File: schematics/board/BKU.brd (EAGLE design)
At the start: 94 x 94 mm, 81 parts, among them Q1 8MHz, Q2 32,768KHz, U1 STM32F405RGT6

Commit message: Папка с платами
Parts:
- removed BT1: 6.8MM_COIN_CELL, SparkFun-Batteries:BATTCON-6.8MM
- removed C10, C11: 10pF, rcl:C0603
- removed C13, C9: 2,2µ, rcl:C0603
- removed C18, C2, C20, C53, C54, C55: 100nF, rcl:C0603
- removed C19: 10µ, rcl:C1206
- removed C7, C8: 27pF, rcl:C0603
- removed D1: BB141, diode:SOD523
- removed GPS: GPSNEO6M, CanCubeSat:GPS-NEO6M
- removed LED2, LED3: (no value), led:CHIPLED_0603
- removed MAG: (no value), pinheadCS:1X04
- removed Q1: 8MHz, 9C-8.000MEEJ-T:XTAL_9C-8.000MEEJ-T
- removed Q2: 32,768KHz, CanCubeSat:C005R
- removed R1, R14, R3, R7: 10k, resistor:R0603
- removed R15, R16: 2k, resistor:R0603
- removed R17: 1M, resistor:R0603
- removed R25, R26: 5k1, resistor:R0603
- removed R4: 620R, resistor:R0603
- removed U$4: USB-C, CanCubeSat:USB-C
- removed U1: STM32F405RGT6, STM32F405RGT6:QFP50P1200X1200X160-64N
- moved JP1 33.6 mm to (8.75, 15.2), turned to 90 degrees
- moved BSK2A 6.50 mm to (9.90, 53.0)
- moved R29 5.02 mm to (49.5, 41.2), turned to 180 degrees
- moved U$6 4.00 mm to (0.00, 34.0)
- moved U$8 2.97 mm to (75.2, 31.8), turned to 90 degrees
- moved BSK2 2.50 mm to (39.0, 9.90)
- moved BSK3 2.50 mm to (84.1, 47.0)
- moved BSK4 2.50 mm to (47.0, 84.1)
- moved C12 2.24 mm to (44.4, 17.2)
- moved R18 2.24 mm to (44.4, 13.0)
- moved R21 2.24 mm to (44.4, 15.1)
- moved R22 2.24 mm to (47.5, 17.2)
- moved R23 2.24 mm to (47.5, 15.1)
- moved R24 2.24 mm to (47.5, 13.0)
- moved RADIO 2.00 mm to (78.2, 41.0)
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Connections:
- removed net N$1: BT1.+, R4.1
- removed net N$15: C8.1, Q1.1, R17.1, U1.6
- removed net N$2: D1.C, R4.2, U1.1
- removed net N$30: C7.1, Q1.2, R17.2, U1.5
- removed net N$34: C10.1, Q2.P$2, U1.3
- removed net N$35: C11.1, Q2.P$1, U1.4
- removed net N$37: LED2.C, R15.2
- removed net N$38: R15.1, U1.53
- removed net N$40: LED3.C, R16.2
- removed net N$41: GPS.P$2, U1.16
- removed net N$42: GPS.P$3, U1.17
- removed net N$5: JP1.2, R14.1, U1.62
- removed net N$6: U1.54, U1.58
- removed net N$7: C9.2, U1.31
- removed net N$8: C13.2, U1.47
- removed net NRST: R7.1, U$4.NRST/EN, U1.7
- removed net RX-S: U$4.RX0, U1.51
- removed net SCL: MAG.3, R25.2, U1.29
- removed net SDA: MAG.4, R26.2, U1.30
- removed net SWC: R3.1, U$4.SWC/TXD, U1.49
- removed net SWD: R1.1, U$4.SWD/RXD, U1.46
- removed net TIME-G: GPS.P$1, U1.14, U1.23, U1.59
- removed net TX-S: U$4.TX0, U1.52
- net 5V: no longer GPS.P$5
- net DAT0: now also JP1.2
- net GND: now also JP1.1, SD.VSS; no longer BT1.-, C10.2, C11.2, C13.1, C18.1, C19.1, C2.2, C20.1, C53.1, C54.1, C55.1, C7.2, C8.2, C9.1, GPS.P$4, MAG.1, R14.2, R16.1, SD.VDD, U$4.GND0, U$4.GND1, U1.12, U1.18, U1.28, U1.60, U1.63
- net RX-ES: no longer U1.42
- net TIME-ES: no longer U1.22
- net TX-ES: no longer U1.43
- net VDD: now also SD.VDD; no longer C18.2, C19.2, C2.1, C20.2, C53.2, C54.2, C55.2, D1.A, JP1.1, LED2.A, LED3.A, MAG.2, R1.2, R25.1, R26.1, R3.2, R7.2, SD.VSS, U$4.3V3/BUS0, U$4.3V3/BUS1, U1.13, U1.19, U1.32, U1.48, U1.64
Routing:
- net 5V: track 299.4 -> 122.3 mm, vias 14 -> 8
- net VDD: track 466.6 -> 325.5 mm, vias 25 -> 17
- net GND: track 525.3 -> 404.7 mm, vias 28 -> 13
- net 1W: track 211.0 -> 103.9 mm, vias 11 -> 8
- net SDA: track 96.3 -> 0.00 mm, vias 8 -> 0
- net SCL: track 91.1 -> 0.00 mm, vias 10 -> 0
- net NRST: track 58.3 -> 0.00 mm, vias 2 -> 0
- net SCLTM: track 144.6 -> 88.9 mm, vias 6 -> 5
- net N$2: track 52.6 -> 0.00 mm, vias 6 -> 0
- net B1_KEM+: track 55.2 -> 3.43 mm, vias 4 -> 2
- net DS: track 123.4 -> 75.3 mm
- net TIME-G: track 45.6 -> 0.00 mm, vias 3 -> 0
- net B2A_KEM+: track 130.4 -> 86.9 mm, vias 7 -> 3
- net B4_KHEAT: track 55.0 -> 11.5 mm, vias 3 -> 1
- net N$15: track 41.6 -> 0.00 mm, vias 3 -> 0
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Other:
- outline, holes or cut-outs redrawn

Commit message: Сделаны платы CROSSnew, SPIDERnew, BSK2
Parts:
- removed BSK2A: (no value), pinheadCS:1X08
- added BSK1: (no value), pinheadCS:1X20
- BSK3: device pinheadCS:1X12 -> pinheadCS:1X14
- BSK4: device pinheadCS:1X14 -> pinheadCS:1X08
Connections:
- new net 3V3: BSK1.8, BSK3.8
- new net B1-CMD: BSK1.4
- new net B1-KHEAT: BSK1.1
- new net B1-KVCC: BSK1.2
- new net B1-ROZE: BSK1.3
- new net B2-CMD: BSK2.4
- new net B2-KHEAT: BSK2.1
- new net B2-KVCC: BSK2.2
- new net B2-ROZE: BSK2.3
- new net B3-CMD: BSK3.4
- new net B3-KHEAT: BSK3.1
- new net B3-KVCC: BSK3.2
- new net B3-ROZE: BSK3.3
- new net B4-CMD: BSK4.4
- new net B4-KHEAT: BSK4.1
- new net B4-KVCC: BSK4.2
- new net B4-ROZE: BSK4.3
- new net B5-CMD: BSK3.13
- new net B5-KHEAT: BSK3.10
- new net B5-KVCC: BSK3.11
- new net B5-ROZE: BSK3.12
- new net PL1-KVCC: BSK1.15
- new net PL2-KVCC: BSK1.16
- new net PL3-KVCC: BSK1.17
- new net PL4-KVCC: BSK1.18
- new net PL5-KVCC: BSK1.19
- new net PL6-KVCC: BSK1.20
- new net SCL: BSK1.10
- new net SDA: BSK1.12
- new net SINS-KVCC: BSK3.14
- net 1W: now also BSK1.5, BSK2.5, BSK3.5, BSK4.5; no longer BSK2.6, BSK2A.6, BSK3.8, BSK4.14
- net 5V: now also BSK1.7, BSK3.7, BSK4.7; no longer BSK2A.7, BSK3.9, BSK4.2
- net B2A_KEM+: no longer BSK2A.3
- net B2A_KEM-: no longer BSK2A.2
- net B2A_KHEAT: no longer BSK2A.4
- net B2A_KVCC: no longer BSK2A.5
- net B2_KEM+: no longer BSK2.3
- net B2_KEM-: no longer BSK2.2
- net B2_KHEAT: no longer BSK2.4
- net B2_KVCC: no longer BSK2.5
- net B3_KEM+: no longer BSK3.5
- net B3_KEM-: no longer BSK3.4
- net B3_KHEAT: no longer BSK3.6
- net B3_KVCC: no longer BSK3.7
- net B4_KEM+: no longer BSK4.11
- net B4_KEM-: no longer BSK4.10
- net B4_KHEAT: no longer BSK4.12
- net B4_KVCC: no longer BSK4.13
- net B5_KEM+: no longer BSK3.2
- net B5_KEM-: no longer BSK3.1
- net B5_KHEAT: no longer BSK3.11
- net B5_KVCC: no longer BSK3.12
- net BUS+: now also BSK1.6, BSK2.6, BSK3.6, BSK4.6; no longer BSK2.8, BSK2A.8, BSK3.10, BSK4.3
- net GND: now also BSK1.11, BSK1.9, BSK2.8, BSK3.9, BSK4.8; no longer BSK2.1, BSK2A.1, BSK3.3, BSK4.9
- net I2CINT: no longer BSK4.5
- net PL_KVCC: no longer BSK4.8
- net SCLTM: no longer BSK4.7
- net SDATM: no longer BSK4.6
- net TIME: now also BSK1.14; no longer BSK4.4
- net TIME-ES: now also BSK1.13
- net VDD: no longer BSK4.1
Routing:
- net GND: track 404.7 -> 378.1 mm
- net BUS+: track 334.6 -> 321.0 mm
- net B2_KEM-: track 48.8 -> 46.1 mm
- net B5_KVCC: track 45.2 -> 42.8 mm

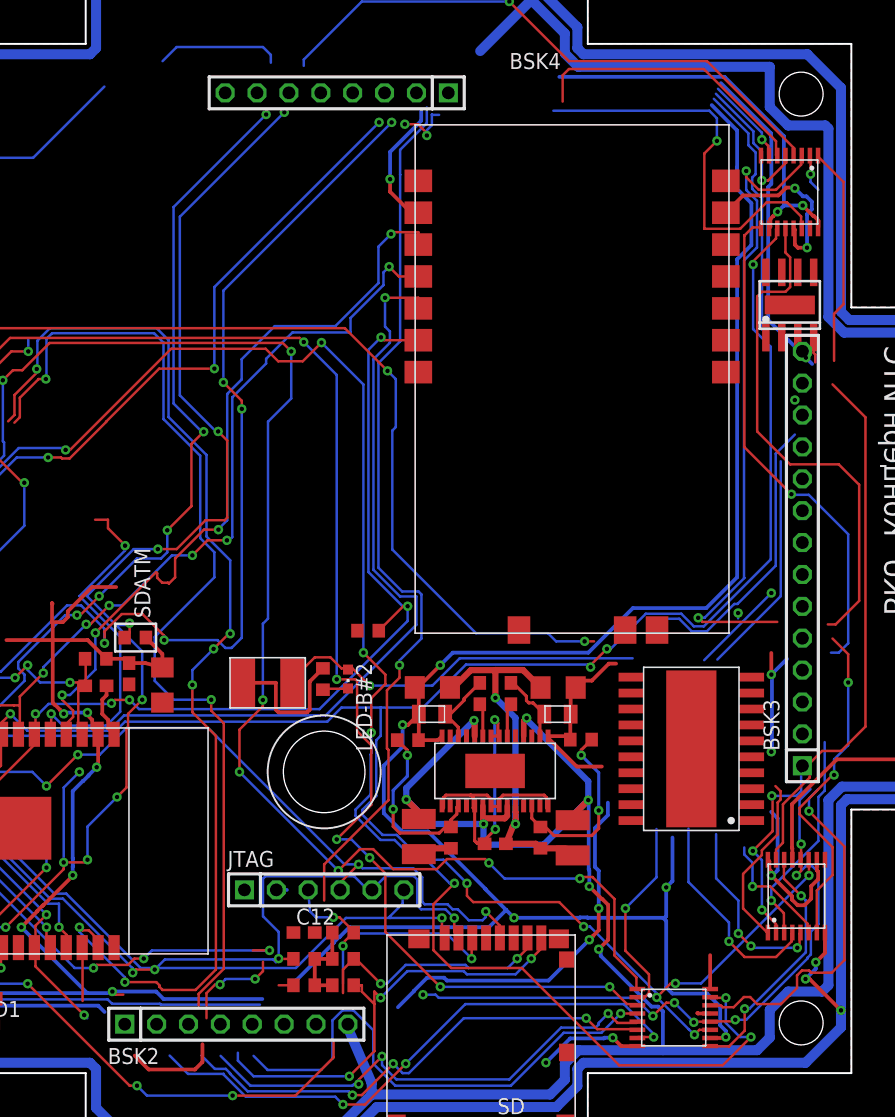
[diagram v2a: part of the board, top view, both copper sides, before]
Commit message: Разведена БСК1
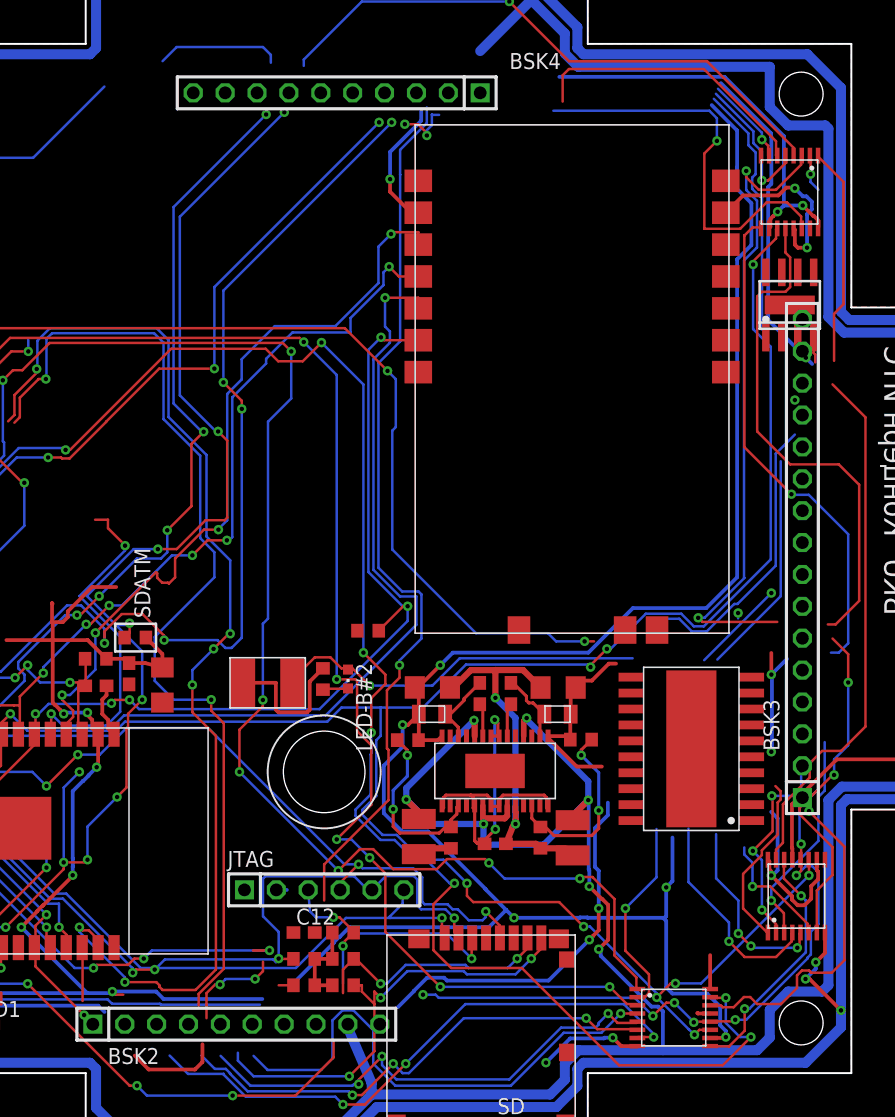
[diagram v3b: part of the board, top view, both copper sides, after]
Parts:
- BSK2, BSK4: device pinheadCS:1X08 -> pinheadCS:1X10
- BSK3: device pinheadCS:1X14 -> pinheadCS:1X16
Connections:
- removed net SCL: BSK1.10
- removed net SCLTM: R10.2, U$13.27
- removed net SDA: BSK1.12
- removed net SDATM: R11.2, U$13.28
- new net SCL-INA: BSK2.9, BSK3.15, BSK4.9
- new net SCL-TM: BSK1.10, R10.2, U$13.27
- new net SDA-INA: BSK2.10, BSK3.16, BSK4.10
- new net SDA-TM: BSK1.12, R11.2, U$13.28
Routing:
- net SDATM: track 100.3 -> 0.00 mm, vias 11 -> 0
- net SDA-TM: track 0.00 -> 100.3 mm, vias 0 -> 11
- net SCLTM: track 88.9 -> 0.00 mm, vias 5 -> 0
- net SCL-TM: track 0.00 -> 88.9 mm, vias 0 -> 5
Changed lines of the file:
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@@
 </autorouter>
 <elements>
-<element name="BSK2" library="pinheadCS" package="1X08" value="" x="39" y="9.9" smashed="yes">
+<element name="BSK2" library="pinheadCS" package="1X10" value="" x="39" y="9.9" smashed="yes">
 <attribute name="NAME" x="28.7638" y="6.7288" size="1.27" layer="25" ratio="10"/>
 <attribute name="VALUE" x="28.84" y="6.725" size="1.27" layer="27"/>
 </element>
-<element name="BSK3" library="pinheadCS" package="1X14" value="" x="84.1" y="47" smashed="yes" rot="R90">
+<element name="BSK3" library="pinheadCS" package="1X16" value="" x="84.1" y="47" smashed="yes" rot="R90">
 <attribute name="NAME" x="82.2712" y="31.6838" size="1.27" layer="25" ratio="10" rot="R90"/>
 <attribute name="VALUE" x="87.275" y="31.76" size="1.27" layer="27" rot="R90"/>
 </element>
-<element name="BSK4" library="pinheadCS" package="1X08" value="" x="47" y="84.1" smashed="yes" rot="R180">
+<element name="BSK4" library="pinheadCS" package="1X10" value="" x="47" y="84.1" smashed="yes" rot="R180">
 <attribute name="NAME" x="64.8562" y="87.2712" size="1.27" layer="25" ratio="10" rot="R180"/>
 <attribute name="VALUE" x="64.78" y="87.275" size="1.27" layer="27" rot="R180"/>
@@
 <wire x1="32.01939375" y1="6.288" x2="30.11" y2="1.2162" width="0" layer="19" extent="1-16"/>
 <wire x1="75.7222375" y1="10.7777625" x2="70.95" y2="8.15" width="0" layer="19" extent="1-1"/>
-<wire x1="47.89" y1="9.9" x2="50.2" y2="3.3" width="0" layer="19" extent="16-16"/>
+<wire x1="45.35" y1="9.9" x2="50.2" y2="3.3" width="0" layer="19" extent="16-16"/>
 <wire x1="69.98" y1="41.3" x2="70.45" y2="33.74" width="0" layer="19" extent="1-1"/>
 <wire x1="72.52" y1="41.3" x2="69.98" y2="41.3" width="0" layer="19" extent="1-1"/>
@@
 <wire x1="56.1" y1="23.91" x2="60.48" y2="24.27" width="0" layer="19" extent="1-1"/>
 <wire x1="61.1" y1="16.77" x2="63.23" y2="23.91" width="0" layer="19" extent="1-1"/>
-<wire x1="43.55" y1="17.2" x2="47.89" y2="9.9" width="0" layer="19" extent="1-1"/>
+<wire x1="43.55" y1="17.2" x2="45.35" y2="9.9" width="0" layer="19" extent="1-1"/>
 <wire x1="39.65" y1="20.6" x2="43.55" y2="17.2" width="0" layer="19" extent="1-1"/>
 <wire x1="48.65" y1="41.25" x2="56.02" y2="36.73" width="0" layer="19" extent="1-1"/>
@@
 <wire x1="28.66" y1="36.86" x2="30.46" y2="36.97" width="0" layer="19" extent="1-1"/>
 <wire x1="29.26" y1="16" x2="30.90739375" y2="7.4" width="0" layer="19" extent="1-1"/>
-<wire x1="38.11" y1="84.1" x2="43.19" y2="93" width="0" layer="19" extent="16-16"/>
+<wire x1="40.65" y1="84.1" x2="43.19" y2="93" width="0" layer="19" extent="16-16"/>
 <wire x1="21.76" y1="25.51" x2="28.79" y2="33.47" width="0" layer="19" extent="1-1"/>
 <wire x1="11.75" y1="30.215" x2="21.76" y2="25.51" width="0" layer="19" extent="1-1"/>
 <wire x1="7.1" y1="37.2" x2="9.4" y2="35.5" width="0" layer="19" extent="1-1"/>
 <wire x1="7.1" y1="30.8" x2="9.55" y2="33.3136" width="0" layer="19" extent="1-16"/>
-<wire x1="84.1" y1="50.81" x2="72.52" y2="41.3" width="0" layer="19" extent="1-1"/>
+<wire x1="84.1" y1="48.27" x2="72.52" y2="41.3" width="0" layer="19" extent="1-1"/>
 <wire x1="53.5" y1="77.09" x2="66.1738" y2="87.657775" width="0" layer="19" extent="1-16"/>
 <wire x1="53.5" y1="61.85" x2="53.5" y2="77.09" width="0" layer="19" extent="1-1"/>
@@
 <contactref element="BSK4" pad="7"/>
 <contactref element="BSK3" pad="7"/>
-<wire x1="84.1" y1="45.73" x2="84.875" y2="62.5" width="0" layer="19" extent="16-16"/>
-<wire x1="81.625" y1="39.475" x2="84.1" y2="45.73" width="0" layer="19" extent="1-1"/>
+<wire x1="84.1" y1="43.19" x2="84.875" y2="62.5" width="0" layer="19" extent="16-16"/>
+<wire x1="81.625" y1="39.475" x2="84.1" y2="43.19" width="0" layer="19" extent="1-1"/>
 <wire x1="80.05" y1="37.55" x2="81.625" y2="37.75" width="0" layer="19" extent="1-1"/>
 <wire x1="80.05" y1="26.12" x2="81.55" y2="31.525" width="0" layer="19" extent="1-1"/>
@@
 <wire x1="68.6014" y1="27.5514" x2="68.125" y2="30.425" width="0" layer="19" extent="1-16"/>
 <wire x1="70.45" y1="26.12" x2="68.6014" y2="26.5514" width="0" layer="19" extent="1-16"/>
-<wire x1="45.35" y1="9.9" x2="51.875" y2="11.25" width="0" layer="19" extent="16-16"/>
-<wire x1="28.5" y1="10.875" x2="45.35" y2="9.9" width="0" layer="19" extent="16-16"/>
+<wire x1="42.81" y1="9.9" x2="51.875" y2="11.25" width="0" layer="19" extent="16-16"/>
+<wire x1="28.5" y1="10.875" x2="42.81" y2="9.9" width="0" layer="19" extent="16-16"/>
 <wire x1="53.7282" y1="82.75163125" x2="77.60483125" y2="84.875" width="0" layer="19" extent="16-16"/>
-<wire x1="40.65" y1="84.1" x2="51.25" y2="79.39516875" width="0" layer="19" extent="16-16"/>
+<wire x1="43.19" y1="84.1" x2="51.25" y2="79.39516875" width="0" layer="19" extent="16-16"/>
 <wire x1="9.9" y1="61.89" x2="7.5" y2="25.5" width="0" layer="19" extent="1-1"/>
 </signal>
@@
 <contactref element="BSK3" pad="5"/>
 <wire x1="80.8875" y1="65.2375" x2="85" y2="64.6" width="0" layer="19" extent="1-16"/>
-<wire x1="84.1" y1="40.65" x2="85.125" y2="62.625" width="0" layer="19" extent="1-1"/>
-<wire x1="45.73" y1="84.1" x2="77.043625" y2="83.625" width="0" layer="19" extent="16-16"/>
-<wire x1="28.49" y1="84.6" x2="45.73" y2="84.1" width="0" layer="19" extent="16-16"/>
+<wire x1="84.1" y1="38.11" x2="85.125" y2="62.625" width="0" layer="19" extent="1-1"/>
+<wire x1="48.27" y1="84.1" x2="77.043625" y2="83.625" width="0" layer="19" extent="16-16"/>
+<wire x1="28.49" y1="84.6" x2="48.27" y2="84.1" width="0" layer="19" extent="16-16"/>
 <wire x1="9.9" y1="66.97" x2="13" y2="66.625" width="0" layer="19" extent="16-16"/>
 <wire x1="5.5" y1="56.125" x2="13" y2="63.75" width="0" layer="19" extent="1-1"/>
 <wire x1="12" y1="37.125" x2="7.375" y2="43.25" width="0" layer="19" extent="16-16"/>
-<wire x1="40.27" y1="9.9" x2="27.125" y2="10.375" width="0" layer="19" extent="16-16"/>
+<wire x1="37.73" y1="9.9" x2="27.125" y2="10.375" width="0" layer="19" extent="16-16"/>
 </signal>
 <signal name="N$3">
@@
 <contactref element="BSK2" pad="6"/>
 <contactref element="BSK3" pad="6"/>
-<wire x1="58.43" y1="87.43" x2="43.19" y2="84.1" width="0" layer="19" extent="16-16"/>
+<wire x1="58.43" y1="87.43" x2="45.73" y2="84.1" width="0" layer="19" extent="16-16"/>
 <wire x1="7.1" y1="31.6" x2="8.5" y2="31.47" width="0" layer="19" extent="1-16"/>
 <wire x1="7.1" y1="36.4" x2="7.1" y2="31.6" width="0" layer="19" extent="1-1"/>
-<wire x1="42.81" y1="9.9" x2="47.89" y2="9.601315625" width="0" layer="19" extent="16-16"/>
-<wire x1="84.1" y1="43.19" x2="92.1206" y2="39.1632" width="0" layer="19" extent="16-16"/>
+<wire x1="40.27" y1="9.9" x2="47.89" y2="9.601315625" width="0" layer="19" extent="16-16"/>
+<wire x1="84.1" y1="40.65" x2="92.1206" y2="39.1632" width="0" layer="19" extent="16-16"/>
 <wire x1="9.9" y1="64.43" x2="8.5" y2="42.71" width="0" layer="19" extent="16-16"/>
 </signal>
@@
 <wire x1="25.7218" y1="54.9718" x2="28.625" y2="57.875" width="0.2" layer="1"/>
 </signal>
-<signal name="SCLTM">
+<signal name="SCL-TM">
 <contactref element="U$13" pad="27"/>
 <wire x1="15.25" y1="15" x2="15.25" y2="16" width="0.2" layer="1"/>
@@
 <wire x1="50.325" y1="46.2656875" x2="50.325" y2="62.5718" width="0.2" layer="16"/>
 <wire x1="50.325" y1="62.5718" x2="52.0532" y2="64.3" width="0.2" layer="16"/>
+<contactref element="BSK1" pad="10"/>
 <wire x1="41.125" y1="14.875" x2="46" y2="19.75" width="0" layer="19" extent="1-1"/>
 <wire x1="16.25" y1="9.125" x2="36.625" y2="10.375" width="0" layer="19" extent="1-16"/>
-</signal>
-<signal name="SDATM">
+<wire x1="9.9" y1="54.27" x2="15.29" y2="16" width="0" layer="19" extent="1-1"/>
+</signal>
+<signal name="SDA-TM">
 <contactref element="U$13" pad="28"/>
 <wire x1="16.625" y1="16.75" x2="16.625" y2="16" width="0.2" layer="1"/>
@@
 <wire x1="30.5" y1="41.85" x2="30.5" y2="41.1" width="0.2" layer="1"/>
 <wire x1="30.5" y1="41.1" x2="30.1" y2="40.7" width="0.2" layer="1"/>
+<contactref element="BSK1" pad="12"/>
+<wire x1="27.0925" y1="44.0175" x2="9.9" y2="49.19" width="0" layer="19" extent="16-16"/>
 </signal>
 <signal name="B1_KEM-">
@@
 <contactref element="BSK1" pad="8"/>
 <contactref element="BSK3" pad="8"/>
-<wire x1="9.9" y1="59.35" x2="84.1" y2="48.27" width="0" layer="19" extent="1-1"/>
-</signal>
-<signal name="SCL">
-<contactref element="BSK1" pad="10"/>
-</signal>
-<signal name="SDA">
-<contactref element="BSK1" pad="12"/>
+<wire x1="9.9" y1="59.35" x2="84.1" y2="45.73" width="0" layer="19" extent="1-1"/>
 </signal>
 <signal name="PL6-KVCC">
@@
 <contactref element="BSK3" pad="14"/>
 </signal>
+<signal name="SCL-INA">
+<contactref element="BSK2" pad="9"/>
+<contactref element="BSK3" pad="15"/>
+<contactref element="BSK4" pad="9"/>
+<wire x1="38.11" y1="84.1" x2="84.1" y2="63.51" width="0" layer="19" extent="1-1"/>
+<wire x1="47.89" y1="9.9" x2="84.1" y2="63.51" width="0" layer="19" extent="1-1"/>
+</signal>
+<signal name="SDA-INA">
+<contactref element="BSK2" pad="10"/>
+<contactref element="BSK3" pad="16"/>
+<contactref element="BSK4" pad="10"/>
+<wire x1="35.57" y1="84.1" x2="84.1" y2="66.05" width="0" layer="19" extent="1-1"/>
+<wire x1="50.43" y1="9.9" x2="84.1" y2="66.05" width="0" layer="19" extent="1-1"/>
+</signal>
 </signals>
